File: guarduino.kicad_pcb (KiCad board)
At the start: 2 copper layers, 99.1 x 99.1 mm, 115 parts, among them M1 PT2272, M2 PT2272, P1 4way mini DIN, P10 GS009S, P11 3pin 3.5mm jack, P12 3pin 3.5mm jack, P13 3pin 3.5mm jack, P14 3pin 3.5mm jack, P2 4way connector, P3 GS009S, P4 GS009S, P5 GS009S, P6 GS009S, P7 GS009S, P8 GS009S, P9 GS009S, Q1 CJ2302, Q10 FDN340P, Q2 PSMN6R0, Q3 PSMN6R0, Q4 PSMN6R0, Q5 PSMN6R0, Q6 PSMN6R0, Q7 PSMN6R0, Q8 PSMN6R0, Q9 PSMN6R0, U1 DS1339, U2 24AA16T, U3 74AHCT244, U4 MCP9700, U5 74AHC1G02, U6 74HCT165, U7 74AHCT1G125, Y1 32.768kHz

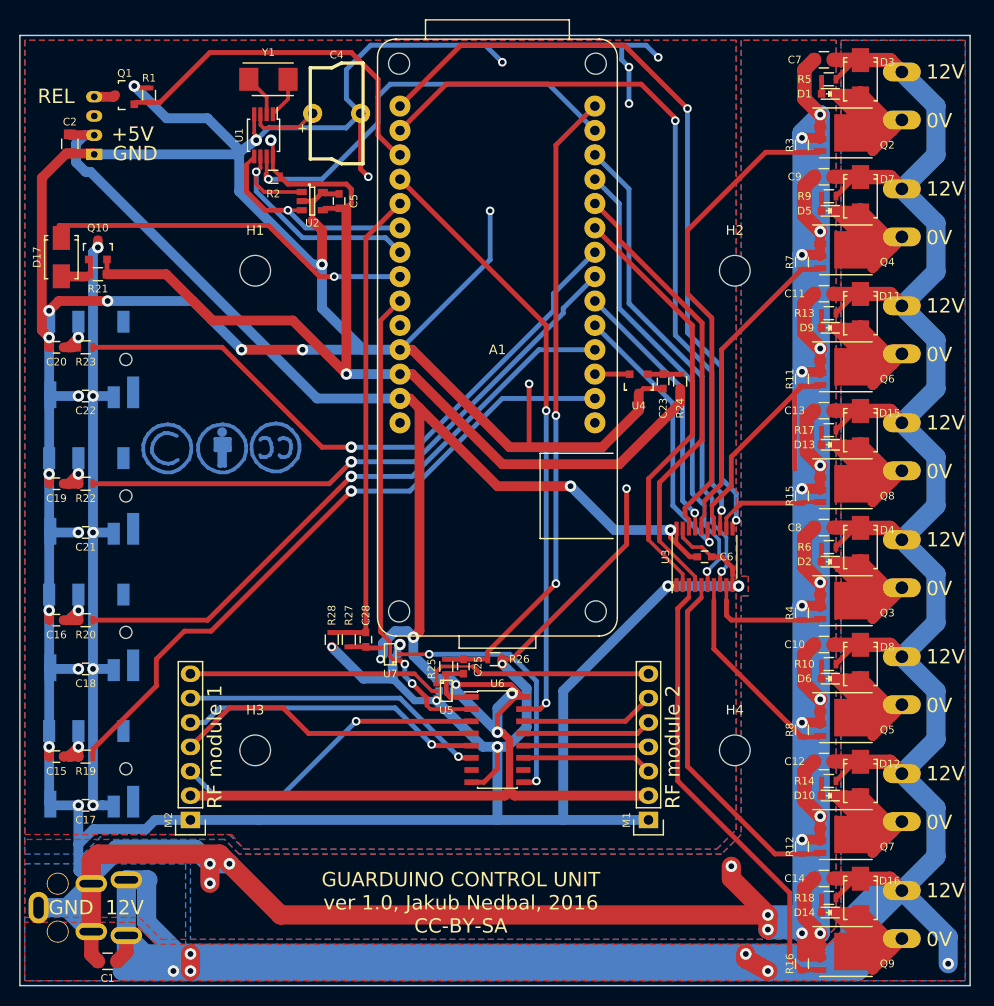
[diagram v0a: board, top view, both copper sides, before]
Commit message: Flipped C6 onto the bottom layer so it doesn't clash with U3
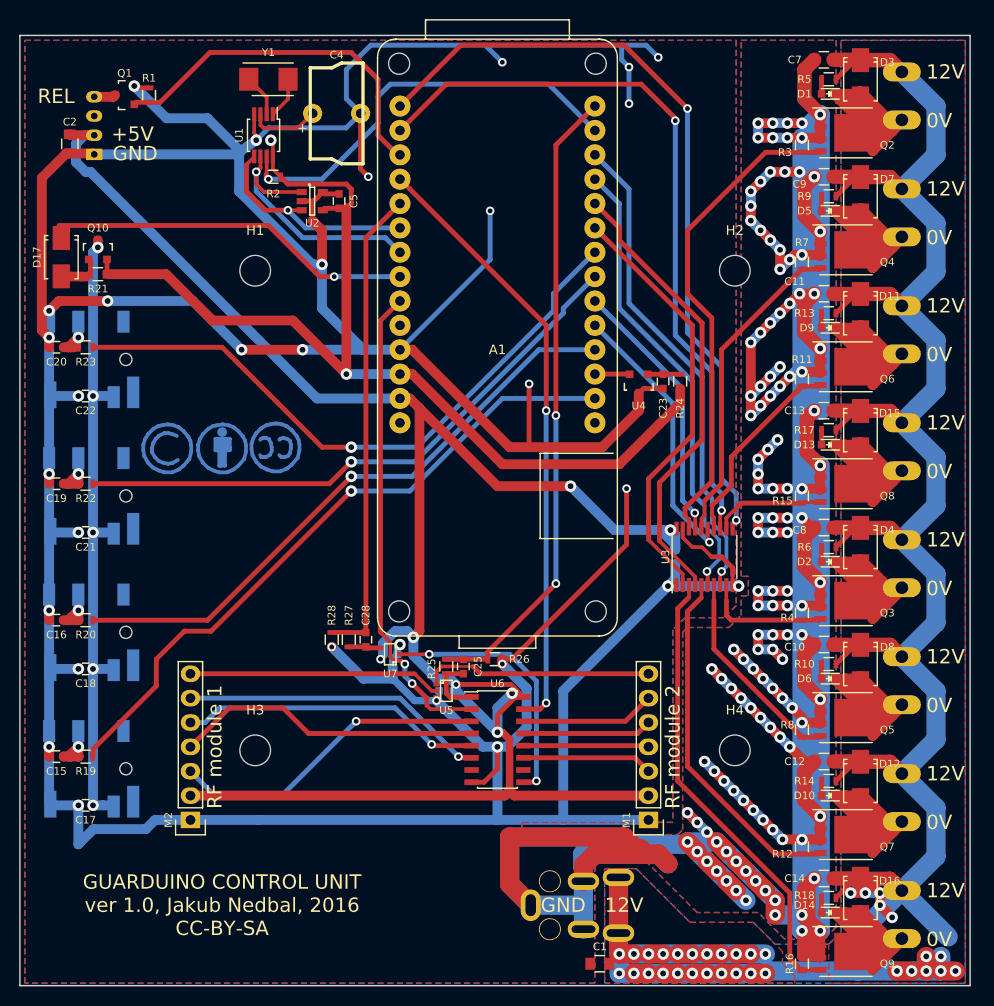
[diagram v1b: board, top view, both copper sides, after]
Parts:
- C6: moved to B.Cu
- moved C1 51.3 mm to (104.1, 124.2)
- moved P1 51.3 mm to (91.4, 118.1)
- moved C6 3.05 mm to (112.0, 81.8), turned to 270 degrees
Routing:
- net GND: track 927.2 -> 1059.7 mm, vias 52 -> 155
- net +12V: track 408.6 -> 284.2 mm, vias 6 -> 34
- net /PowerDrivers/OUT2: track 29.7 -> 21.9 mm
